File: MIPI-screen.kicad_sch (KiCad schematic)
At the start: 41 parts, among them U201 TPS65131RGE, U202 TLV62568DBV, U203 LP3320B6F

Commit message: essential routing done
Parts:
- removed D201, D202, D203: D_Schottky, symbol Device:D_Schottky
- added D201, D202, D203: CUS10S40_H3F, footprints:SOD-323_L1.7-W1.3-LS2.5-RD, symbol CUS10S40_H3F:CUS10S40_H3F
- C201, C202, C203, C204, C205, C206, C207, C208, C209, C210, C211, C213, C215: footprint (none) -> Capacitor_SMD:C_0603_1608Metric
- C212, C216: value 10uF/10V -> 10uF/25V; footprint (none) -> Capacitor_SMD:C_0603_1608Metric
- C214: value 4.7uF/10V -> 4.7uF/50V; footprint (none) -> Capacitor_SMD:C_0603_1608Metric
- JP201, JP202, JP203, JP204: footprint (none) -> Jumper:SolderJumper-2_P1.3mm_Open_RoundedPad1.0x1.5mm
- JP205: footprint (none) -> Jumper:SolderJumper-3_P1.3mm_Open_RoundedPad1.0x1.5mm
- R201, R202, R203, R204, R205, R206, R207, R208, R209: footprint (none) -> Resistor_SMD:R_0402_1005Metric
- TP201: footprint (none) -> TestPoint:TestPoint_Pad_D1.5mm
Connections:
- net LED_PWR.A: now also D203.1 (K)
- net at C203.1, C204.1, C205.1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: now also D202.1 (K)
- net at C207.2, C210.2, C211.2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: now also D201.2 (A)
- net at L204.2, U203.1 (LX): now also D203.2 (A)
- net at L202.2, U201.13 (OUTN), U201.14 (OUTN): now also D201.1 (K)
- net at L201.2, U201.1 (INP), U201.24 (INP): now also D202.2 (A)
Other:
- note added: "LED driver"

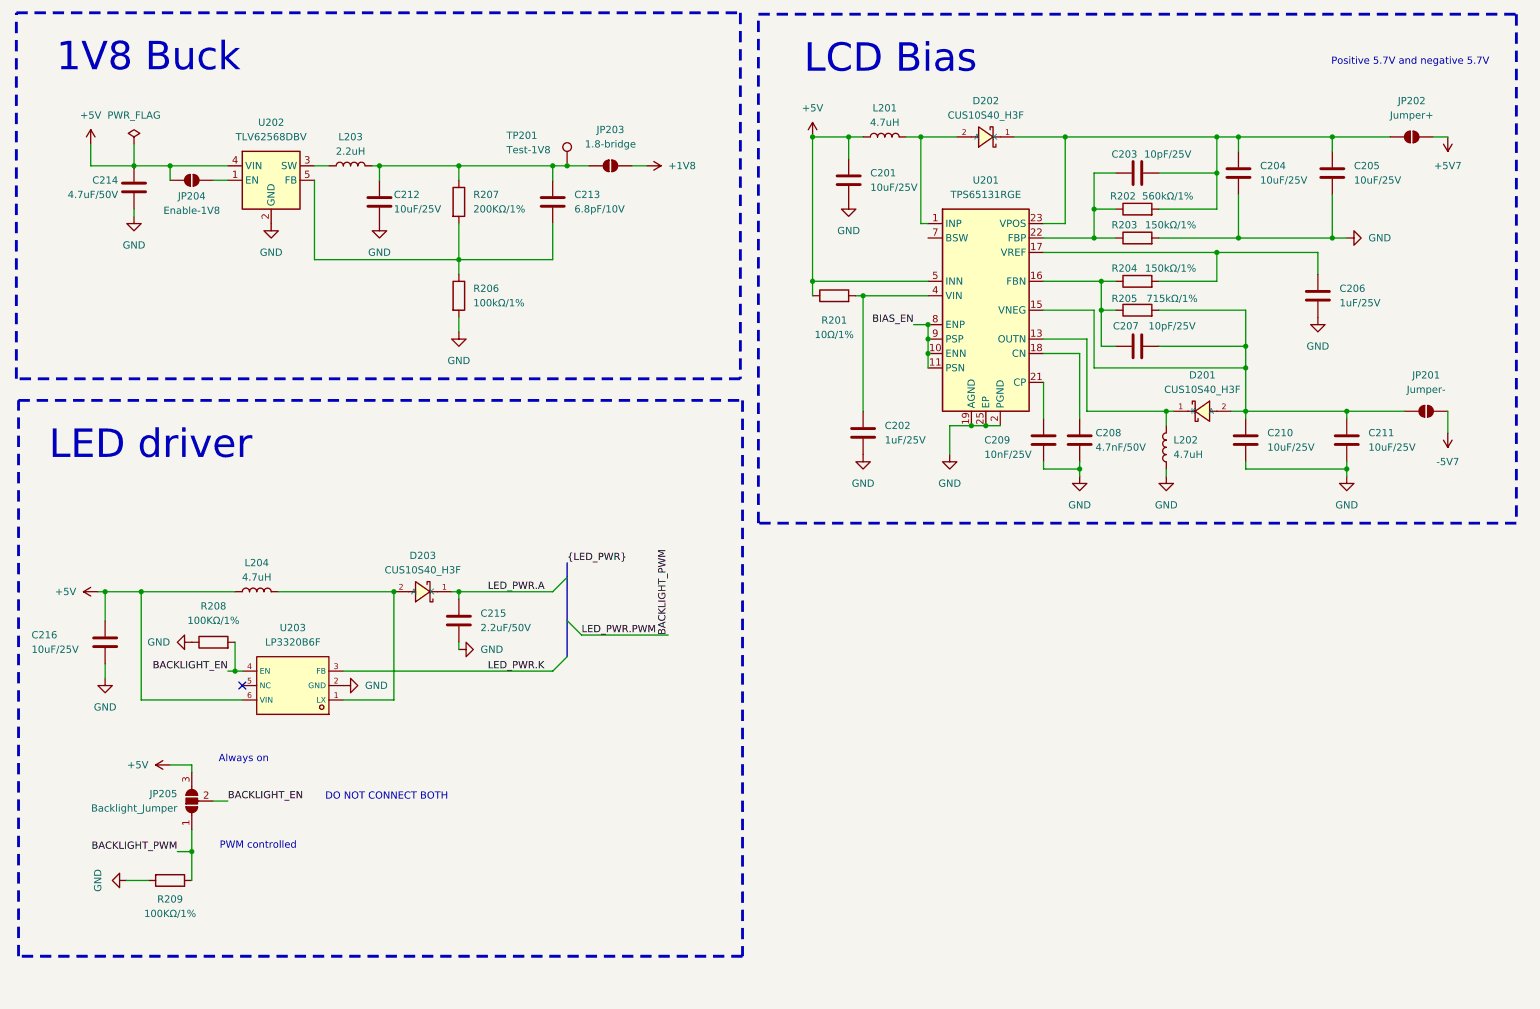
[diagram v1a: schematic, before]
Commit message: 1v8 buck and 4.7uh inductor
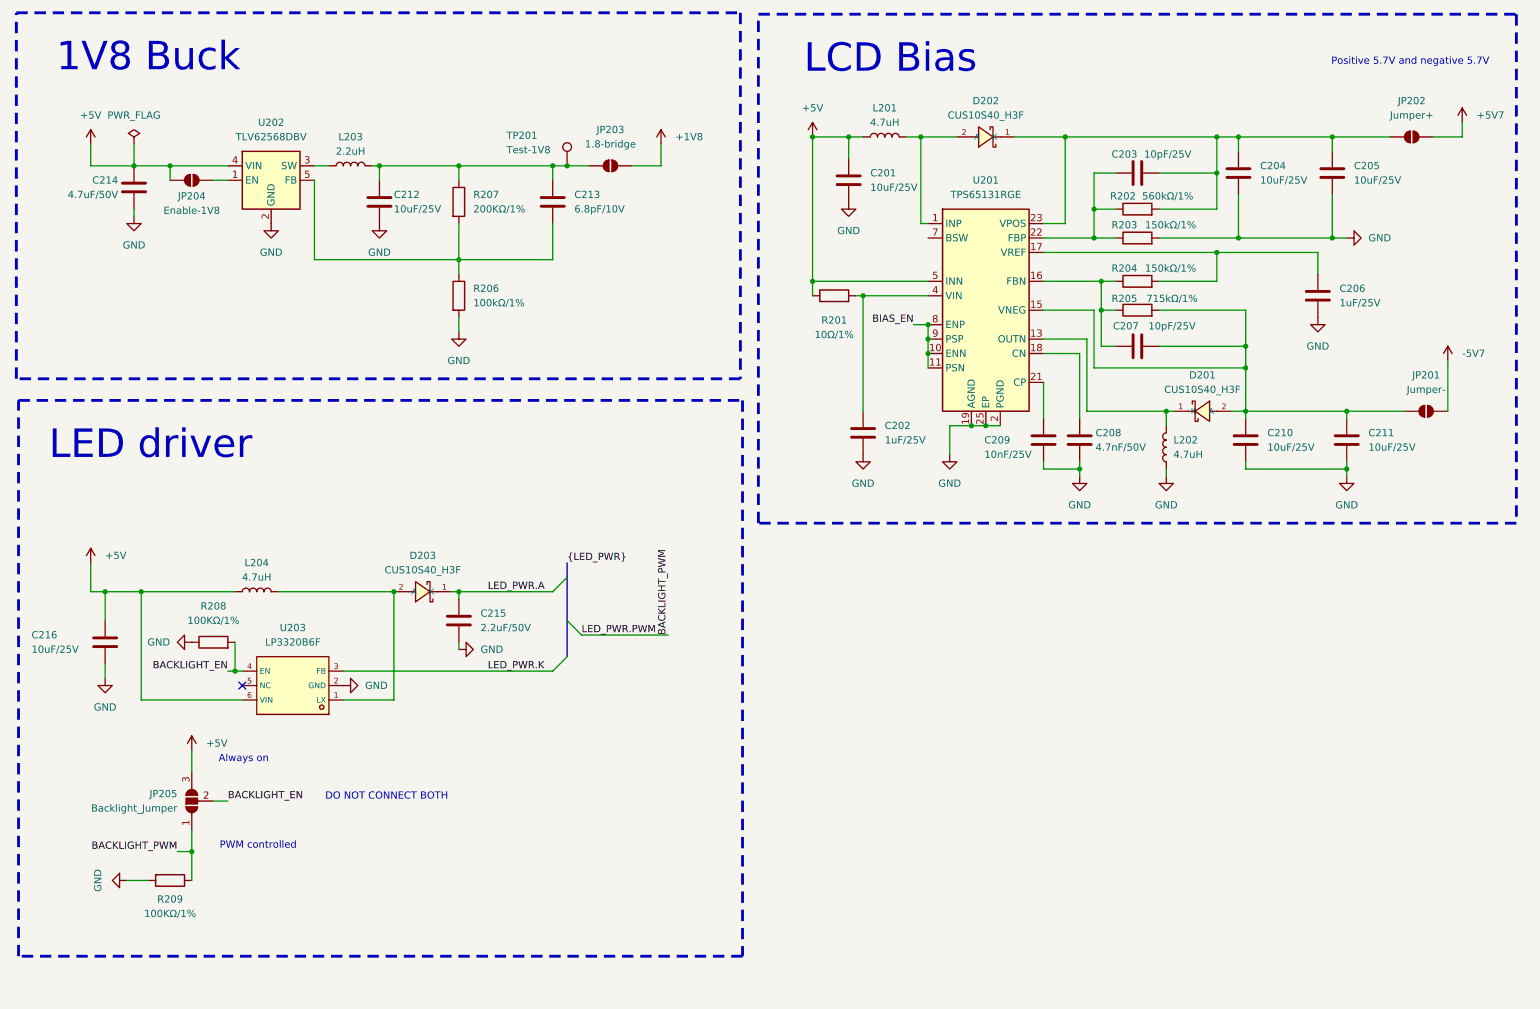
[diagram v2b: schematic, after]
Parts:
- JP205: now in the parts list

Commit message: init layout
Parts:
- removed C201, C204, C205, C210, C211: 10uF/25V, Capacitor_SMD:C_0603_1608Metric, symbol Device:C
- removed C202, C206: 1uF/25V, Capacitor_SMD:C_0603_1608Metric, symbol Device:C
- removed C203, C207: 10pF/25V, Capacitor_SMD:C_0603_1608Metric, symbol Device:C
- removed C208: 4.7nF/50V, Capacitor_SMD:C_0603_1608Metric, symbol Device:C
- removed C209: 10nF/25V, Capacitor_SMD:C_0603_1608Metric, symbol Device:C
- removed D201, D202, D203: CUS10S40_H3F, footprints:SOD-323_L1.7-W1.3-LS2.5-RD, symbol CUS10S40_H3F:CUS10S40_H3F
- removed JP201: Jumper-, Jumper:SolderJumper-2_P1.3mm_Open_RoundedPad1.0x1.5mm, symbol Jumper:SolderJumper_2_Open
- removed JP202: Jumper+, Jumper:SolderJumper-2_P1.3mm_Open_RoundedPad1.0x1.5mm, symbol Jumper:SolderJumper_2_Open
- removed L201, L202: 4.7uH, symbol Device:L
- removed L203: 2.2uH, symbol Device:L
- removed R201: 10Ω/1%, Resistor_SMD:R_0402_1005Metric, symbol Device:R
- removed R202: 560kΩ/1%, Resistor_SMD:R_0402_1005Metric, symbol Device:R
- removed R203, R204: 150kΩ/1%, Resistor_SMD:R_0402_1005Metric, symbol Device:R
- removed R205: 715kΩ/1%, Resistor_SMD:R_0402_1005Metric, symbol Device:R
- removed R206: 100kΩ/1%, Resistor_SMD:R_0402_1005Metric, symbol Device:R
- removed R207: 200KΩ/1%, Resistor_SMD:R_0402_1005Metric, symbol Device:R
- removed R208: 100KΩ/1%, Resistor_SMD:R_0402_1005Metric, symbol Device:R
- removed U201: TPS65131RGE, Package_DFN_QFN:VQFN-24-1EP_4x4mm_P0.5mm_EP2.45x2.45mm_ThermalVias, symbol Regulator_Switching:TPS65131RGE
- removed U202: TLV62568DBV, Package_TO_SOT_SMD:SOT-23-5, symbol Regulator_Switching:TLV62568DBV
- added C220, C221, C222, C223: 4.7uF/16V, Capacitor_SMD:C_0603_1608Metric, symbol Device:C
- added D403: B5817WS_C7420329, footprints:SOD-323_L1.7-W1.3-LS2.5-FD, symbol B5817WS_C7420329:B5817WS_C7420329
- added JP208: +5.7_bridge, Connector_PinHeader_2.54mm:PinHeader_1x02_P2.54mm_Vertical, symbol Jumper:SolderJumper_2_Open
- added JP209: -5v7_bridge, Connector_PinHeader_2.54mm:PinHeader_1x02_P2.54mm_Vertical, symbol Jumper:SolderJumper_2_Open
- added JP210: Jumper+, Connector_PinHeader_2.54mm:PinHeader_1x02_P2.54mm_Vertical, symbol Jumper:SolderJumper_2_Open
- added JP211: Jumper-, Connector_PinHeader_2.54mm:PinHeader_1x02_P2.54mm_Vertical, symbol Jumper:SolderJumper_2_Open
- added L206, L207: 4.7uH, footprints:IND-SMD_L2.5-W2.0_SPH252012, symbol Device:L
- added NT201: NetTie_GND, NetTie:NetTie-2_SMD_Pad0.5mm, symbol Device:NetTie_2
- added TP203: TestPoint_GND_PAD, TestPoint:TestPoint_THTPad_D2.0mm_Drill1.0mm, symbol Connector:TestPoint
- added TP204: TestPoint_GNDA_PAD, TestPoint:TestPoint_THTPad_D2.0mm_Drill1.0mm, symbol Connector:TestPoint
- added TP205: TestPoint_anode, TestPoint:TestPoint_THTPad_D2.0mm_Drill1.0mm, symbol Connector:TestPoint
- added TP206: TestPoint_cathode, TestPoint:TestPoint_THTPad_D2.0mm_Drill1.0mm, symbol Connector:TestPoint
- added TP207: TestPoint_PWM, TestPoint:TestPoint_THTPad_D2.0mm_Drill1.0mm, symbol Connector:TestPoint
- added TP208: TestPoint_P_5V7, TestPoint:TestPoint_THTPad_D2.0mm_Drill1.0mm, symbol Connector:TestPoint
- added TP209: TestPoint_N_5V7, TestPoint:TestPoint_THTPad_D2.0mm_Drill1.0mm, symbol Connector:TestPoint
- added U202: TPS65132WRVCR_C2876379, footprints:WQFN-20_L4.0-W3.0-P0.50-BL-EP, symbol TPS65132WRVCR_C2876379:TPS65132WRVCR_C2876379
- added U204: MCP1603T-180I/OS, TSOT5_MC_MCH, symbol MCP1603T_180I_OS:MCP1603T-180I_OS
- C212: value 10uF/25V -> 4.7uF/16V
- C213: value 6.8pF/10V -> 2.2uF/50V; footprint Capacitor_SMD:C_0603_1608Metric -> Capacitor_SMD:C_0805_2012Metric
- C214: value 4.7uF/50V -> 4.7uF/16V
- C215: footprint Capacitor_SMD:C_0603_1608Metric -> Capacitor_SMD:C_0805_2012Metric
- JP203, JP204: footprint Jumper:SolderJumper-2_P1.3mm_Open_RoundedPad1.0x1.5mm -> Connector_PinHeader_2.54mm:PinHeader_1x02_P2.54mm_Vertical
- JP205: footprint Jumper:SolderJumper-3_P1.3mm_Open_RoundedPad1.0x1.5mm -> Connector_PinHeader_2.54mm:PinHeader_1x03_P2.54mm_Vertical; now left out of the parts list
- L204: footprint (none) -> footprints:IND-SMD_L2.5-W2.0_SPH252012
- TP201: footprint TestPoint:TestPoint_Pad_D1.5mm -> TestPoint:TestPoint_THTPad_D2.0mm_Drill1.0mm
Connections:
- net +5V7: now also JP210.2 (B)
- net -5V7: now also JP211.2 (B)
- net BACKLIGHT_PWM: now also TP207.1
- net GND: now also C220.2, C221.2, C222.2, C223.2, NT201.1, TP203.1, U202.1 (PGND), U202.11 (PGND), U202.12 (PGND), U202.2 (PGND), U202.21 (EP), U204.2 (GND)
- net LED_PWR.A: now also D403.2 (K), TP205.1
- net LED_PWR.K: now also TP206.1
- net at C212.1, JP203.1 (A), TP201.1: now also L206.2, U204.4 (VFB/VOUT); no longer C213.1
- net at C213.2: now also U202.13 (CFLY1)
- net at JP204.1 (A): now also U204.3 (*SHDN)
- net at L204.2, U203.1 (LX): now also D403.1 (A)
- net +5V renamed +3V3
- net +3V3: now also C223.1, JP208.1 (A), JP209.2 (B), L207.1, U202.4 (VIN), U204.1 (VIN)
- new net: JP208.2 (B), U202.5 (ENP)
- new net: L206.1, U204.5 (LX)
- new net: C222.1, U202.14 (REG), U202.18 (REG)
- new net: C213.1, U202.10 (CFLY2)
- new net: JP209.1 (A), U202.6 (ENN)
- new net GNDA: NT201.2, TP204.1, U202.17 (AGND), U202.3 (AGND)
- new net OUTN: C220.1, JP211.1 (A), TP209.1, U202.9 (OUTN)
- new net OUTP: C221.1, JP210.1 (A), TP208.1, U202.15 (OUTP), U202.16 (OUTP)
- new net SCL_3V3: U202.7 (SDA)
- new net SDA_3V3: U202.8 (SCL)
- new net SW: L207.2, U202.19 (SW), U202.20 (SW)
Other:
- moved on the sheet: C212, C214, R209

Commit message: board fabbed
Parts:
- added R206: 5.1Ω/1%, Resistor_SMD:R_0805_2012Metric, symbol Device:R
- L204: Field4 (none) -> SPH252012H4R7MT
- U204: footprint TSOT5_MC_MCH -> footprints:TSOT5_MC_MCH
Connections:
- net GND: now also R206.2
- net LED_PWR.K: now also R206.1
- net BACKLIGHT_PWM renamed LED_PWM
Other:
- moved on the sheet: TP206
